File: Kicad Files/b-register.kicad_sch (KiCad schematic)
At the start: 20 parts

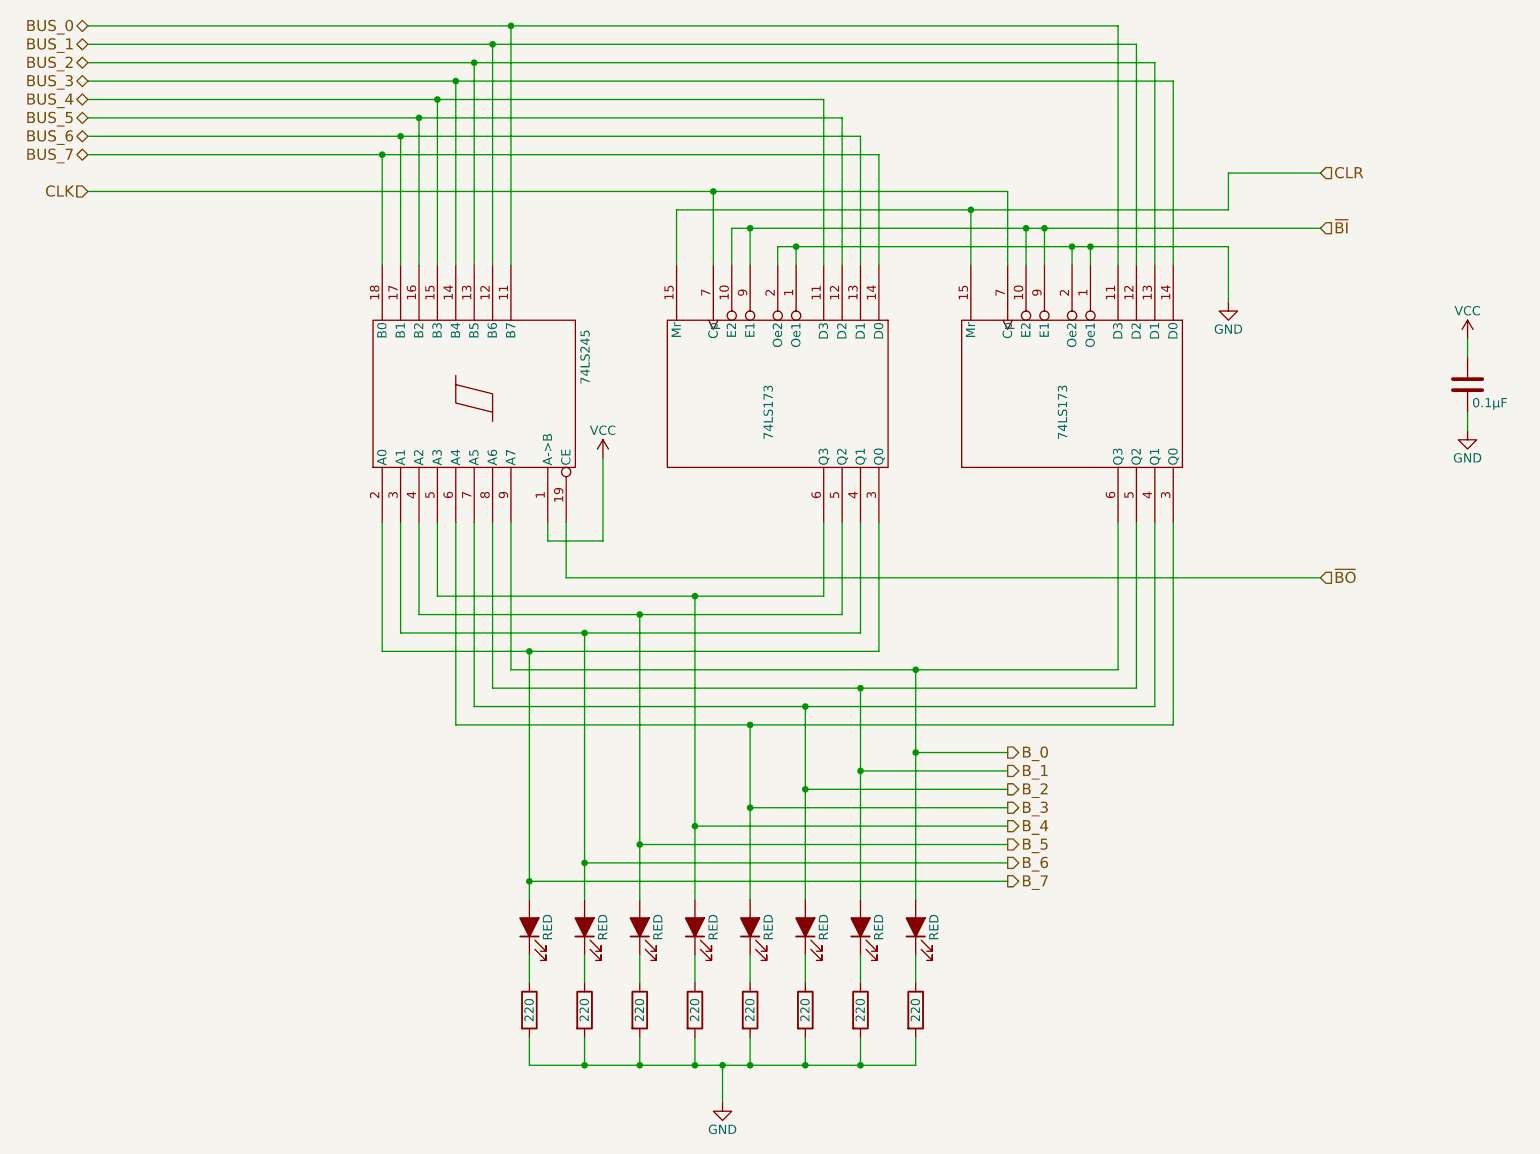
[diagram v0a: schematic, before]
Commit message: started tidy up in control
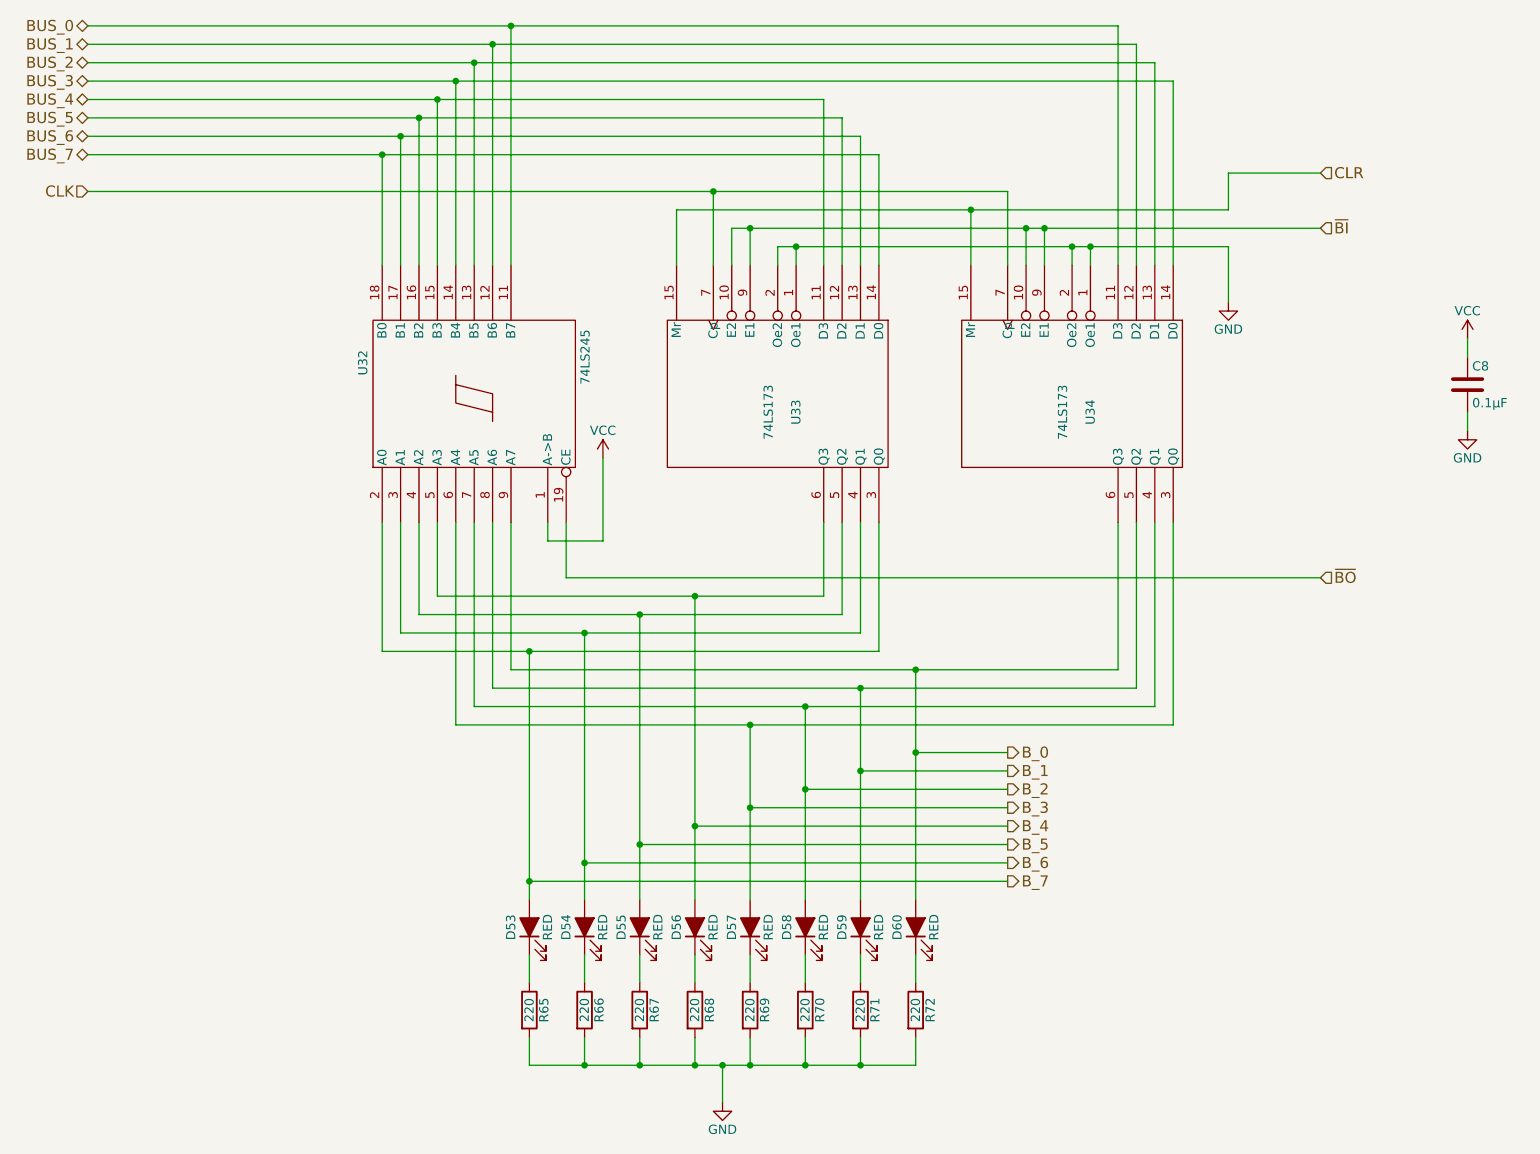
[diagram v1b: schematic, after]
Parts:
- gave numbers to parts that had none: 20
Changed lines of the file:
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@@
   (symbol (lib_id "8bit-computer-rescue:74LS173-8bit-computer-rescue") (at 173.99 66.04 270) (unit 1)
     (in_bom yes) (on_board yes)
-    (property "Reference" "" (id 0) (at 176.53 68.58 0))
+    (property "Reference" "U34" (id 0) (at 176.53 68.58 0))
     (property "Value" "74LS173" (id 1) (at 172.72 68.58 0))
     (property "Footprint" "Package_DIP:DIP-16_W7.62mm" (id 2) (at 173.99 66.04 0)
@@
   (symbol (lib_id "8bit-computer-rescue:74LS245-8bit-computer-rescue") (at 91.44 66.04 90) (unit 1)
     (in_bom yes) (on_board yes)
-    (property "Reference" "" (id 0) (at 76.835 63.5 0)
+    (property "Reference" "U32" (id 0) (at 76.835 63.5 0)
       (effects (font (size 1.27 1.27)) (justify left bottom))
     )
@@
   (symbol (lib_id "8bit-computer-rescue:LED_ALT-Device") (at 106.68 139.7 90) (unit 1)
     (in_bom yes) (on_board yes)
-    (property "Reference" "" (id 0) (at 104.14 139.7 0))
+    (property "Reference" "D54" (id 0) (at 104.14 139.7 0))
     (property "Value" "RED" (id 1) (at 109.22 139.7 0))
     (property "Footprint" "LED_THT:LED_D5.0mm" (id 2) (at 106.68 139.7 0)
@@
   (symbol (lib_id "Device:R") (at 99.06 151.13 0) (unit 1)
     (in_bom yes) (on_board yes)
-    (property "Reference" "" (id 0) (at 101.092 151.13 90))
+    (property "Reference" "R65" (id 0) (at 101.092 151.13 90))
     (property "Value" "220" (id 1) (at 99.06 151.13 90))
     (property "Footprint" "Resistor_THT:R_Axial_DIN0207_L6.3mm_D2.5mm_P7.62mm_Horizontal" (id 2) (at 97.282 151.13 90)
@@
   (symbol (lib_id "Device:R") (at 106.68 151.13 0) (unit 1)
     (in_bom yes) (on_board yes)
-    (property "Reference" "" (id 0) (at 108.712 151.13 90))
+    (property "Reference" "R66" (id 0) (at 108.712 151.13 90))
     (property "Value" "220" (id 1) (at 106.68 151.13 90))
     (property "Footprint" "Resistor_THT:R_Axial_DIN0207_L6.3mm_D2.5mm_P7.62mm_Horizontal" (id 2) (at 104.902 151.13 90)
@@
   (symbol (lib_id "Device:R") (at 144.78 151.13 0) (unit 1)
     (in_bom yes) (on_board yes)
-    (property "Reference" "" (id 0) (at 146.812 151.13 90))
+    (property "Reference" "R71" (id 0) (at 146.812 151.13 90))
     (property "Value" "220" (id 1) (at 144.78 151.13 90))
     (property "Footprint" "Resistor_THT:R_Axial_DIN0207_L6.3mm_D2.5mm_P7.62mm_Horizontal" (id 2) (at 143.002 151.13 90)
@@
   (symbol (lib_id "8bit-computer-rescue:74LS173-8bit-computer-rescue") (at 133.35 66.04 270) (unit 1)
     (in_bom yes) (on_board yes)
-    (property "Reference" "" (id 0) (at 135.89 68.58 0))
+    (property "Reference" "U33" (id 0) (at 135.89 68.58 0))
     (property "Value" "74LS173" (id 1) (at 132.08 68.58 0))
     (property "Footprint" "Package_DIP:DIP-16_W7.62mm" (id 2) (at 133.35 66.04 0)
@@
   (symbol (lib_id "8bit-computer-rescue:LED_ALT-Device") (at 99.06 139.7 90) (unit 1)
     (in_bom yes) (on_board yes)
-    (property "Reference" "" (id 0) (at 96.52 139.7 0))
+    (property "Reference" "D53" (id 0) (at 96.52 139.7 0))
     (property "Value" "RED" (id 1) (at 101.6 139.7 0))
     (property "Footprint" "LED_THT:LED_D5.0mm" (id 2) (at 99.06 139.7 0)
@@
   (symbol (lib_id "8bit-computer-rescue:LED_ALT-Device") (at 114.3 139.7 90) (unit 1)
     (in_bom yes) (on_board yes)
-    (property "Reference" "" (id 0) (at 111.76 139.7 0))
+    (property "Reference" "D55" (id 0) (at 111.76 139.7 0))
     (property "Value" "RED" (id 1) (at 116.84 139.7 0))
     (property "Footprint" "LED_THT:LED_D5.0mm" (id 2) (at 114.3 139.7 0)
@@
   (symbol (lib_id "8bit-computer-rescue:LED_ALT-Device") (at 121.92 139.7 90) (unit 1)
     (in_bom yes) (on_board yes)
-    (property "Reference" "" (id 0) (at 119.38 139.7 0))
+    (property "Reference" "D56" (id 0) (at 119.38 139.7 0))
     (property "Value" "RED" (id 1) (at 124.46 139.7 0))
     (property "Footprint" "LED_THT:LED_D5.0mm" (id 2) (at 121.92 139.7 0)
@@
   (symbol (lib_id "8bit-computer-rescue:LED_ALT-Device") (at 129.54 139.7 90) (unit 1)
     (in_bom yes) (on_board yes)
-    (property "Reference" "" (id 0) (at 127 139.7 0))
+    (property "Reference" "D57" (id 0) (at 127 139.7 0))
     (property "Value" "RED" (id 1) (at 132.08 139.7 0))
     (property "Footprint" "LED_THT:LED_D5.0mm" (id 2) (at 129.54 139.7 0)
@@
   (symbol (lib_id "8bit-computer-rescue:LED_ALT-Device") (at 137.16 139.7 90) (unit 1)
     (in_bom yes) (on_board yes)
-    (property "Reference" "" (id 0) (at 134.62 139.7 0))
+    (property "Reference" "D58" (id 0) (at 134.62 139.7 0))
     (property "Value" "RED" (id 1) (at 139.7 139.7 0))
     (property "Footprint" "LED_THT:LED_D5.0mm" (id 2) (at 137.16 139.7 0)
@@
   (symbol (lib_id "8bit-computer-rescue:LED_ALT-Device") (at 144.78 139.7 90) (unit 1)
     (in_bom yes) (on_board yes)
-    (property "Reference" "" (id 0) (at 142.24 139.7 0))
+    (property "Reference" "D59" (id 0) (at 142.24 139.7 0))
     (property "Value" "RED" (id 1) (at 147.32 139.7 0))
     (property "Footprint" "LED_THT:LED_D5.0mm" (id 2) (at 144.78 139.7 0)
@@
   (symbol (lib_id "8bit-computer-rescue:LED_ALT-Device") (at 152.4 139.7 90) (unit 1)
     (in_bom yes) (on_board yes)
-    (property "Reference" "" (id 0) (at 149.86 139.7 0))
+    (property "Reference" "D60" (id 0) (at 149.86 139.7 0))
     (property "Value" "RED" (id 1) (at 154.94 139.7 0))
     (property "Footprint" "LED_THT:LED_D5.0mm" (id 2) (at 152.4 139.7 0)
@@
   (symbol (lib_id "Device:R") (at 114.3 151.13 0) (unit 1)
     (in_bom yes) (on_board yes)
-    (property "Reference" "" (id 0) (at 116.332 151.13 90))
+    (property "Reference" "R67" (id 0) (at 116.332 151.13 90))
     (property "Value" "220" (id 1) (at 114.3 151.13 90))
     (property "Footprint" "Resistor_THT:R_Axial_DIN0207_L6.3mm_D2.5mm_P7.62mm_Horizontal" (id 2) (at 112.522 151.13 90)
@@
   (symbol (lib_id "Device:R") (at 121.92 151.13 0) (unit 1)
     (in_bom yes) (on_board yes)
-    (property "Reference" "" (id 0) (at 123.952 151.13 90))
+    (property "Reference" "R68" (id 0) (at 123.952 151.13 90))
     (property "Value" "220" (id 1) (at 121.92 151.13 90))
     (property "Footprint" "Resistor_THT:R_Axial_DIN0207_L6.3mm_D2.5mm_P7.62mm_Horizontal" (id 2) (at 120.142 151.13 90)
@@
   (symbol (lib_id "Device:R") (at 129.54 151.13 0) (unit 1)
     (in_bom yes) (on_board yes)
-    (property "Reference" "" (id 0) (at 131.572 151.13 90))
+    (property "Reference" "R69" (id 0) (at 131.572 151.13 90))
     (property "Value" "220" (id 1) (at 129.54 151.13 90))
     (property "Footprint" "Resistor_THT:R_Axial_DIN0207_L6.3mm_D2.5mm_P7.62mm_Horizontal" (id 2) (at 127.762 151.13 90)
@@
   (symbol (lib_id "Device:R") (at 137.16 151.13 0) (unit 1)
     (in_bom yes) (on_board yes)
-    (property "Reference" "" (id 0) (at 139.192 151.13 90))
+    (property "Reference" "R70" (id 0) (at 139.192 151.13 90))
     (property "Value" "220" (id 1) (at 137.16 151.13 90))
     (property "Footprint" "Resistor_THT:R_Axial_DIN0207_L6.3mm_D2.5mm_P7.62mm_Horizontal" (id 2) (at 135.382 151.13 90)
@@
   (symbol (lib_id "Device:R") (at 152.4 151.13 0) (unit 1)
     (in_bom yes) (on_board yes)
-    (property "Reference" "" (id 0) (at 154.432 151.13 90))
+    (property "Reference" "R72" (id 0) (at 154.432 151.13 90))
     (property "Value" "220" (id 1) (at 152.4 151.13 90))
     (property "Footprint" "Resistor_THT:R_Axial_DIN0207_L6.3mm_D2.5mm_P7.62mm_Horizontal" (id 2) (at 150.622 151.13 90)
@@
   (symbol (lib_id "Device:C") (at 228.6 64.77 0) (unit 1)
     (in_bom yes) (on_board yes)
-    (property "Reference" "" (id 0) (at 229.235 62.23 0)
+    (property "Reference" "C8" (id 0) (at 229.235 62.23 0)
       (effects (font (size 1.27 1.27)) (justify left))
     )

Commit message: work on cl
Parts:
- C20: renamed from C8; value 0.1µF -> C
- R85: renamed from R65; value 220 -> R
- R86: renamed from R66; value 220 -> R
- R87: renamed from R67; value 220 -> R
- R88: renamed from R68; value 220 -> R
- R89: renamed from R69; value 220 -> R
- R90: renamed from R70; value 220 -> R
- R91: renamed from R71; value 220 -> R
- R92: renamed from R72; value 220 -> R
- renumbered D53 to D50, D54 to D51, D55 to D52, D56 to D53, D57 to D54, D58 to D55, D59 to D56, D60 to D57, U32 to U39, U33 to U40, U34 to U41

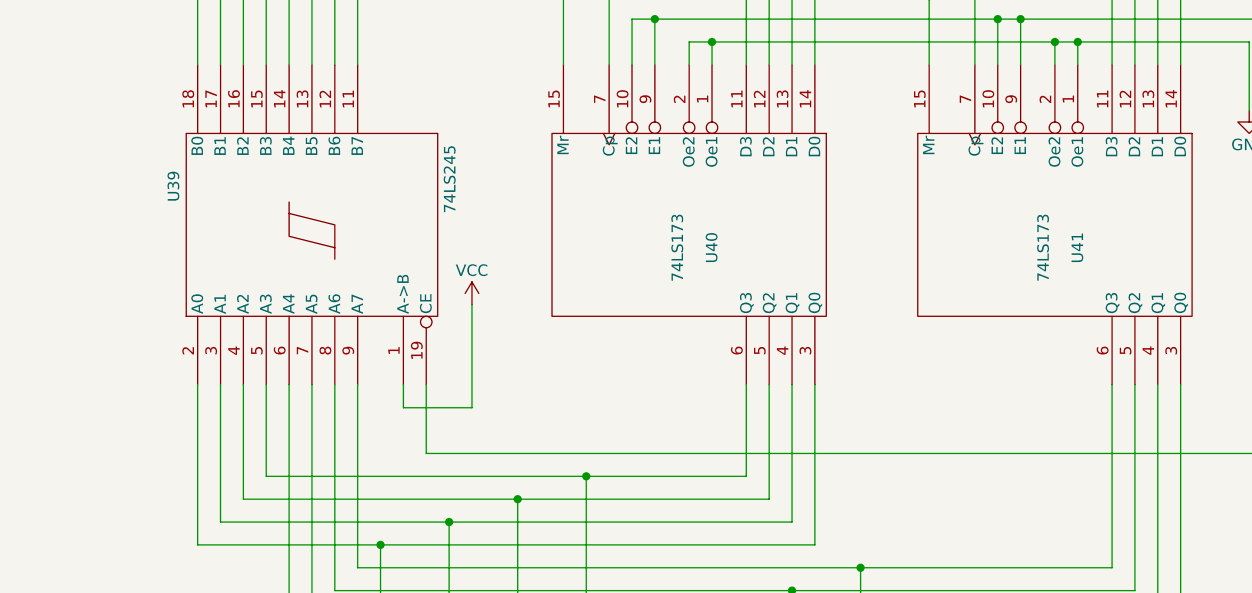
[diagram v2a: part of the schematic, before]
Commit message: fixed ecc problems
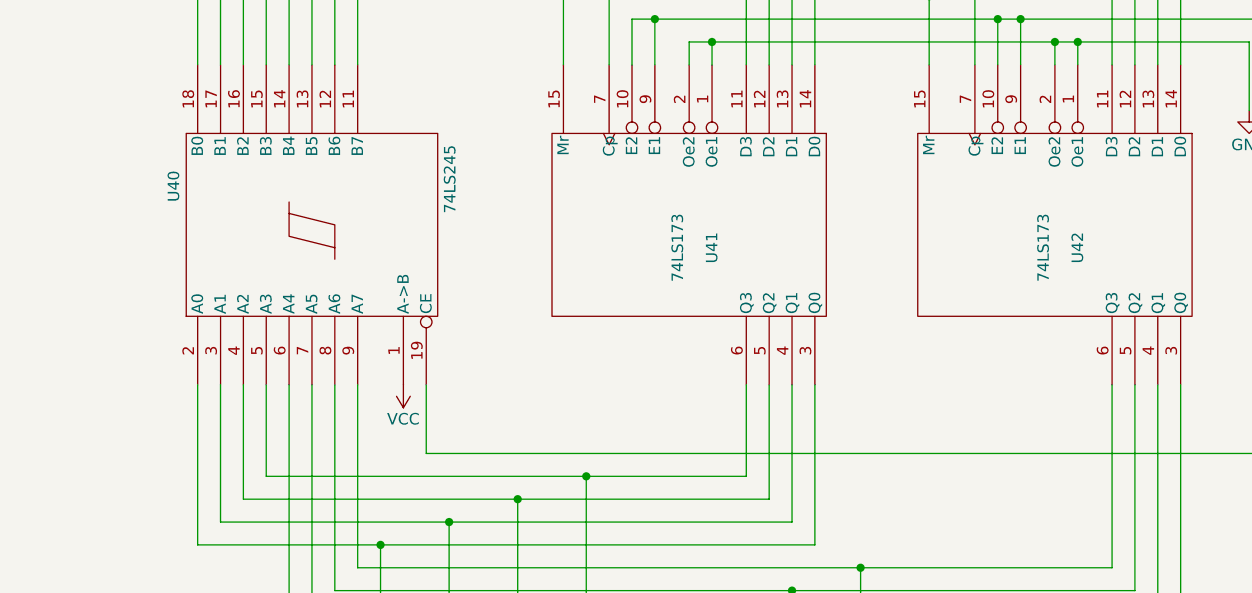
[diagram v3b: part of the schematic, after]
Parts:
- renumbered U39 to U40, U40 to U41, U41 to U42
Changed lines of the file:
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@@
-    (stroke (width 0) (type default) (color 0 0 0 0))
-  )
-  (wire (pts (xy 109.22 86.36) (xy 109.22 74.93))
     (stroke (width 0) (type default) (color 0 0 0 0))
   )
@@
     (stroke (width 0) (type default) (color 0 0 0 0))
   )
-  (wire (pts (xy 101.6 86.36) (xy 109.22 86.36))
-    (stroke (width 0) (type default) (color 0 0 0 0))
-  )
   (wire (pts (xy 86.36 48.26) (xy 86.36 25.4))
     (stroke (width 0) (type default) (color 0 0 0 0))
@@
     (stroke (width 0) (type default) (color 0 0 0 0))
   )
-  (wire (pts (xy 101.6 83.82) (xy 101.6 86.36))
-    (stroke (width 0) (type default) (color 0 0 0 0))
-  )
   (wire (pts (xy 165.1 118.11) (xy 144.78 118.11))
     (stroke (width 0) (type default) (color 0 0 0 0))
@@
   (symbol (lib_id "8bit-computer-rescue:74LS173-8bit-computer-rescue") (at 173.99 66.04 270) (unit 1)
     (in_bom yes) (on_board yes)
-    (property "Reference" "U41" (id 0) (at 176.53 68.58 0))
+    (property "Reference" "U42" (id 0) (at 176.53 68.58 0))
     (property "Value" "74LS173" (id 1) (at 172.72 68.58 0))
     (property "Footprint" "Package_DIP:DIP-16_W7.62mm" (id 2) (at 173.99 66.04 0)
@@
   (symbol (lib_id "8bit-computer-rescue:74LS245-8bit-computer-rescue") (at 91.44 66.04 90) (unit 1)
     (in_bom yes) (on_board yes)
-    (property "Reference" "U39" (id 0) (at 76.835 63.5 0)
+    (property "Reference" "U40" (id 0) (at 76.835 63.5 0)
       (effects (font (size 1.27 1.27)) (justify left bottom))
     )
@@
   (symbol (lib_id "power:GND") (at 125.73 163.83 0) (unit 1)
     (in_bom yes) (on_board yes)
-    (property "Reference" "#PWR0118" (id 0) (at 125.73 170.18 0)
+    (property "Reference" "#PWR0122" (id 0) (at 125.73 170.18 0)
       (effects (font (size 1.27 1.27)) hide)
     )
@@
   (symbol (lib_id "power:GND") (at 195.58 53.34 0) (unit 1)
     (in_bom yes) (on_board yes)
-    (property "Reference" "#PWR0119" (id 0) (at 195.58 59.69 0)
+    (property "Reference" "#PWR0123" (id 0) (at 195.58 59.69 0)
       (effects (font (size 1.27 1.27)) hide)
     )
@@
   (symbol (lib_id "8bit-computer-rescue:74LS173-8bit-computer-rescue") (at 133.35 66.04 270) (unit 1)
     (in_bom yes) (on_board yes)
-    (property "Reference" "U40" (id 0) (at 135.89 68.58 0))
+    (property "Reference" "U41" (id 0) (at 135.89 68.58 0))
     (property "Value" "74LS173" (id 1) (at 132.08 68.58 0))
     (property "Footprint" "Package_DIP:DIP-16_W7.62mm" (id 2) (at 133.35 66.04 0)
@@
     (pin "2")
   )
-  (symbol (lib_id "power:VCC") (at 109.22 74.93 0) (unit 1)
-    (in_bom yes) (on_board yes)
-    (property "Reference" "#PWR0117" (id 0) (at 109.22 78.74 0)
-      (effects (font (size 1.27 1.27)) hide)
-    )
-    (property "Value" "VCC" (id 1) (at 109.22 71.12 0))
-    (property "Footprint" "" (id 2) (at 109.22 74.93 0)
-      (effects (font (size 1.27 1.27)) hide)
-    )
-    (property "Datasheet" "" (id 3) (at 109.22 74.93 0)
+  (symbol (lib_id "power:VCC") (at 101.6 83.82 180) (unit 1)
+    (in_bom yes) (on_board yes)
+    (property "Reference" "#PWR0121" (id 0) (at 101.6 80.01 0)
+      (effects (font (size 1.27 1.27)) hide)
+    )
+    (property "Value" "VCC" (id 1) (at 101.6 87.63 0))
+    (property "Footprint" "" (id 2) (at 101.6 83.82 0)
+      (effects (font (size 1.27 1.27)) hide)
+    )
+    (property "Datasheet" "" (id 3) (at 101.6 83.82 0)
       (effects (font (size 1.27 1.27)) hide)
     )
@@
   (symbol (lib_id "power:VCC") (at 228.6 58.42 0) (unit 1)
     (in_bom yes) (on_board yes)
-    (property "Reference" "#PWR0120" (id 0) (at 228.6 62.23 0)
+    (property "Reference" "#PWR0124" (id 0) (at 228.6 62.23 0)
       (effects (font (size 1.27 1.27)) hide)
     )
@@
   (symbol (lib_id "power:GND") (at 228.6 71.12 0) (unit 1)
     (in_bom yes) (on_board yes)
-    (property "Reference" "#PWR0121" (id 0) (at 228.6 77.47 0)
-      (effects (font (size 1.27 1.27)) hide)
-    )
+    (property "Reference" "#PWR0125" (id 0) (at 228.6 77.47 0)
+      (effects (font (size 1.27 1.27)) hide)
+    )
